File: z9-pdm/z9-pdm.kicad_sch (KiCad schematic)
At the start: 8 parts

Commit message: x
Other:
- sheet buzzer renamed shared_buzzer
- sheet usb renamed shared_usb
- sheet shared_buzzer: file buzzer.kicad_sch -> ../z9-shared/shared_buzzer.kicad_sch
- sheet shared_usb: file usb.kicad_sch -> ../z9-shared/shared_usbc.kicad_sch
- moved on the sheet: H5, H6, H7, H8
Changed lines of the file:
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@@
+		)
+	)
+	(label "USB_OTG_FS_VBUS"
+		(at 95.25 260.35 0)
+		(effects
+			(font
+				(size 1.27 1.27)
+			)
+			(justify left bottom)
 		)
 	)
@@
 		)
 	)
-	(label "USB_OTG_FS_VBUS"
-		(at 96.52 44.45 0)
-		(effects
-			(font
-				(size 1.27 1.27)
-			)
-			(justify left bottom)
-		)
-	)
 	(label "VIPOWER_DI1"
 		(at 52.07 69.85 180)
@@
 		)
 	)
-	(label "USB_OTG_FS_DP"
-		(at 96.52 29.21 0)
-		(effects
-			(font
-				(size 1.27 1.27)
-			)
-			(justify left bottom)
-		)
-	)
 	(label "SENSE_7"
 		(at 312.42 80.01 180)
@@
 		)
 	)
+	(label "USB_OTG_FS_DP"
+		(at 95.25 245.11 0)
+		(effects
+			(font
+				(size 1.27 1.27)
+			)
+			(justify left bottom)
+		)
+	)
 	(label "VIPOWER_SDI"
 		(at 52.07 80.01 180)
@@
 		)
 	)
-	(label "USB_OTG_FS_DM"
-		(at 96.52 34.29 0)
-		(effects
-			(font
-				(size 1.27 1.27)
-			)
-			(justify left bottom)
-		)
-	)
 	(label "SENSE_2"
 		(at 312.42 149.86 180)
@@
 	(label "CAN1_RX"
 		(at 191.77 180.34 0)
+		(effects
+			(font
+				(size 1.27 1.27)
+			)
+			(justify left bottom)
+		)
+	)
+	(label "USB_OTG_FS_DM"
+		(at 95.25 250.19 0)
 		(effects
 			(font
@@
 		(fields_autoplaced yes)
 		(property "Reference" "H2"
-			(at 401.32 227.3299 0)
+			(at 401.32 228.5999 0)
 			(effects
 				(font
@@
 				)
 				(justify left)
+				(hide yes)
 			)
 		)
@@
 	(symbol
 		(lib_id "dnt_global:MountingHole_-_4MM")
-		(at 389.89 236.22 0)
+		(at 372.11 236.22 0)
 		(unit 1)
 		(exclude_from_sim yes)
@@
 		(fields_autoplaced yes)
 		(property "Reference" "H6"
-			(at 392.43 234.9499 0)
+			(at 374.65 236.2199 0)
 			(effects
 				(font
@@
 		)
 		(property "Value" "MountingHole_-_4MM"
-			(at 392.43 237.4899 0)
-			(effects
-				(font
-					(size 1.27 1.27)
-				)
-				(justify left)
+			(at 374.65 237.4899 0)
+			(effects
+				(font
+					(size 1.27 1.27)
+				)
+				(justify left)
+				(hide yes)
 			)
 		)
 		(property "Footprint" "MountingHole:MountingHole_4.3mm_M4_DIN965"
-			(at 389.89 236.22 0)
+			(at 372.11 236.22 0)
 			(effects
 				(font
@@
 		)
 		(property "Datasheet" "~"
-			(at 389.89 236.22 0)
+			(at 372.11 236.22 0)
 			(effects
 				(font
@@
 		)
 		(property "Description" "Mounting Hole without connection"
-			(at 389.89 236.22 0)
+			(at 372.11 236.22 0)
 			(effects
 				(font
@@
 	(symbol
 		(lib_id "dnt_global:MountingHole_-_4MM")
-		(at 389.89 243.84 0)
+		(at 372.11 243.84 0)
 		(unit 1)
 		(exclude_from_sim yes)
@@
 		(fields_autoplaced yes)
 		(property "Reference" "H5"
-			(at 392.43 242.5699 0)
+			(at 374.65 243.8399 0)
 			(effects
 				(font
@@
 		)
 		(property "Value" "MountingHole_-_4MM"
-			(at 392.43 245.1099 0)
-			(effects
-				(font
-					(size 1.27 1.27)
-				)
-				(justify left)
+			(at 374.65 245.1099 0)
+			(effects
+				(font
+					(size 1.27 1.27)
+				)
+				(justify left)
+				(hide yes)
 			)
 		)
 		(property "Footprint" "MountingHole:MountingHole_4.3mm_M4_DIN965"
-			(at 389.89 243.84 0)
+			(at 372.11 243.84 0)
 			(effects
 				(font
@@
 		)
 		(property "Datasheet" "~"
-			(at 389.89 243.84 0)
+			(at 372.11 243.84 0)
 			(effects
 				(font
@@
 		)
 		(property "Description" "Mounting Hole without connection"
-			(at 389.89 243.84 0)
+			(at 372.11 243.84 0)
 			(effects
 				(font
@@
 		(fields_autoplaced yes)
 		(property "Reference" "H3"
-			(at 401.32 234.9499 0)
+			(at 401.32 236.2199 0)
 			(effects
 				(font
@@
 				)
 				(justify left)
+				(hide yes)
 			)
 		)
@@
 				)
 				(justify left)
+				(hide yes)
 			)
 		)
@@
 		(fields_autoplaced yes)
 		(property "Reference" "H4"
-			(at 401.32 242.5699 0)
+			(at 401.32 243.8399 0)
 			(effects
 				(font
@@
 				)
 				(justify left)
+				(hide yes)
 			)
 		)
@@
 	(symbol
 		(lib_id "dnt_global:MountingHole_-_4MM")
-		(at 389.89 220.98 0)
+		(at 372.11 220.98 0)
 		(unit 1)
 		(exclude_from_sim yes)
@@
 		(fields_autoplaced yes)
 		(property "Reference" "H8"
-			(at 392.43 219.7099 0)
+			(at 374.65 219.7099 0)
 			(effects
 				(font
@@
 		)
 		(property "Value" "MountingHole_-_4MM"
-			(at 392.43 222.2499 0)
-			(effects
-				(font
-					(size 1.27 1.27)
-				)
-				(justify left)
+			(at 374.65 222.2499 0)
+			(effects
+				(font
+					(size 1.27 1.27)
+				)
+				(justify left)
+				(hide yes)
 			)
 		)
 		(property "Footprint" "MountingHole:MountingHole_4.3mm_M4_DIN965"
-			(at 389.89 220.98 0)
+			(at 372.11 220.98 0)
 			(effects
 				(font
@@
 		)
 		(property "Datasheet" "~"
-			(at 389.89 220.98 0)
+			(at 372.11 220.98 0)
 			(effects
 				(font
@@
 		)
 		(property "Description" "Mounting Hole without connection"
-			(at 389.89 220.98 0)
+			(at 372.11 220.98 0)
 			(effects
 				(font
@@
 	(symbol
 		(lib_id "dnt_global:MountingHole_-_4MM")
-		(at 389.89 228.6 0)
+		(at 372.11 228.6 0)
 		(unit 1)
 		(exclude_from_sim yes)
@@
 		(fields_autoplaced yes)
 		(property "Reference" "H7"
-			(at 392.43 227.3299 0)
+			(at 374.65 227.3299 0)
 			(effects
 				(font
@@
 		)
 		(property "Value" "MountingHole_-_4MM"
-			(at 392.43 229.8699 0)
-			(effects
-				(font
-					(size 1.27 1.27)
-				)
-				(justify left)
+			(at 374.65 229.8699 0)
+			(effects
+				(font
+					(size 1.27 1.27)
+				)
+				(justify left)
+				(hide yes)
 			)
 		)
 		(property "Footprint" "MountingHole:MountingHole_4.3mm_M4_DIN965"
-			(at 389.89 228.6 0)
+			(at 372.11 228.6 0)
 			(effects
 				(font
@@
 		)
 		(property "Datasheet" "~"
-			(at 389.89 228.6 0)
+			(at 372.11 228.6 0)
 			(effects
 				(font
@@
 		)
 		(property "Description" "Mounting Hole without connection"
-			(at 389.89 228.6 0)
+			(at 372.11 228.6 0)
 			(effects
 				(font
@@
 	)
 	(sheet
-		(at 52.07 25.4)
-		(size 44.45 24.13)
+		(at 53.34 241.3)
+		(size 41.91 24.13)
 		(exclude_from_sim no)
 		(in_bom yes)
@@
 			(color 0 0 0 0.0000)
 		)
-		(property "Sheetname" "usb"
-			(at 52.07 24.6884 0)
+		(property "Sheetname" "shared_usb"
+			(at 53.34 240.5884 0)
 			(effects
 				(font
@@
 			)
 		)
-		(property "Sheetfile" "usb.kicad_sch"
-			(at 52.07 50.1146 0)
+		(property "Sheetfile" "../z9-shared/shared_usbc.kicad_sch"
+			(at 53.34 266.0146 0)
 			(effects
 				(font
@@
 		)
 		(pin "USB_OTG_FS_DP" bidirectional
-			(at 96.52 29.21 0)
+			(at 95.25 245.11 0)
 			(effects
 				(font
@@
 		)
 		(pin "USB_OTG_FS_DM" bidirectional
-			(at 96.52 34.29 0)
+			(at 95.25 250.19 0)
 			(effects
 				(font
@@
 		)
 		(pin "USB_OTG_FS_VBUS" output
-			(at 96.52 44.45 0)
+			(at 95.25 260.35 0)
 			(effects
 				(font
@@
 			(color 0 0 0 0.0000)
 		)
-		(property "Sheetname" "buzzer"
+		(property "Sheetname" "shared_buzzer"
 			(at 53.34 217.7284 0)
 			(effects
@@
 			)
 		)
-		(property "Sheetfile" "buzzer.kicad_sch"
+		(property "Sheetfile" "../z9-shared/shared_buzzer.kicad_sch"
 			(at 53.34 230.4546 0)
 			(effects

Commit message: x
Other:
- sheet connectors ports: added OUT_HC_1, OUT_HC_10, OUT_HC_11, OUT_HC_12, OUT_HC_2, OUT_HC_3, OUT_HC_4, OUT_HC_5, OUT_HC_6, OUT_HC_7, OUT_HC_8, OUT_HC_9; removed HC_1, HC_10, HC_11, HC_12, HC_2, HC_3, HC_4, HC_5, HC_6, HC_7, HC_8, HC_9

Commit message: pdm sch drc clean
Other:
- removed sheet can
- added sheet shared_can_isolated (../z9-shared/shared_isolated_can.kicad_sch)
- note removed: "Anode (positive side) and a cathode (negative side)"
- note removed: "git commands git add --all git commit -m "blah" git push"

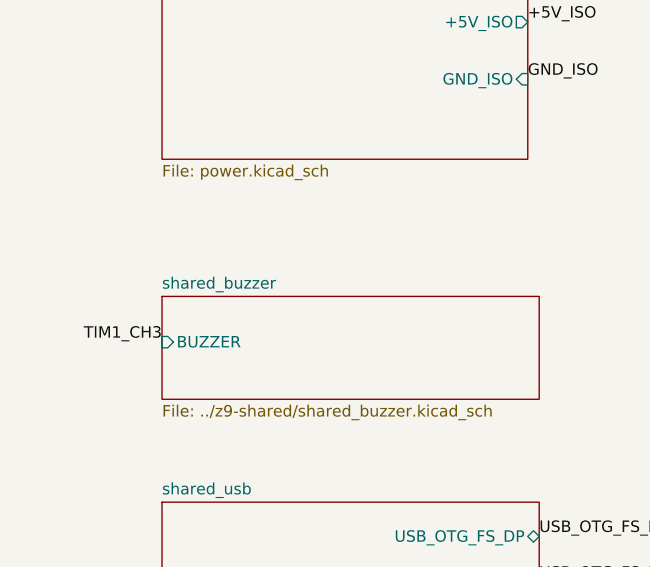
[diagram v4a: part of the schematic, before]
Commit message: reset shared chematics to correct series
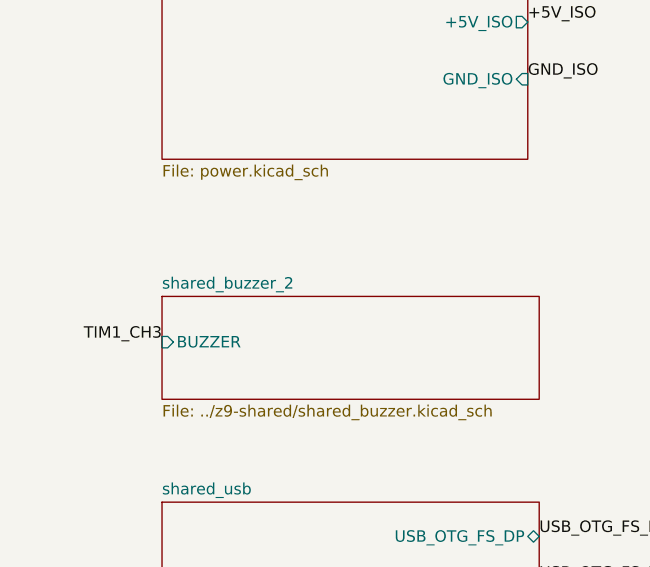
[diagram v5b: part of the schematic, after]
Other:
- sheet shared_buzzer renamed shared_buzzer_2
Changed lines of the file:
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@@
 			(color 0 0 0 0.0000)
 		)
-		(property "Sheetname" "shared_buzzer"
+		(property "Sheetname" "shared_buzzer_2"
 			(at 52.07 173.2784 0)
 			(effects
